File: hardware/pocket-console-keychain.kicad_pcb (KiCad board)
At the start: 2 copper layers, 52 x 76 mm, 15 parts, among them J1 USB-C Power

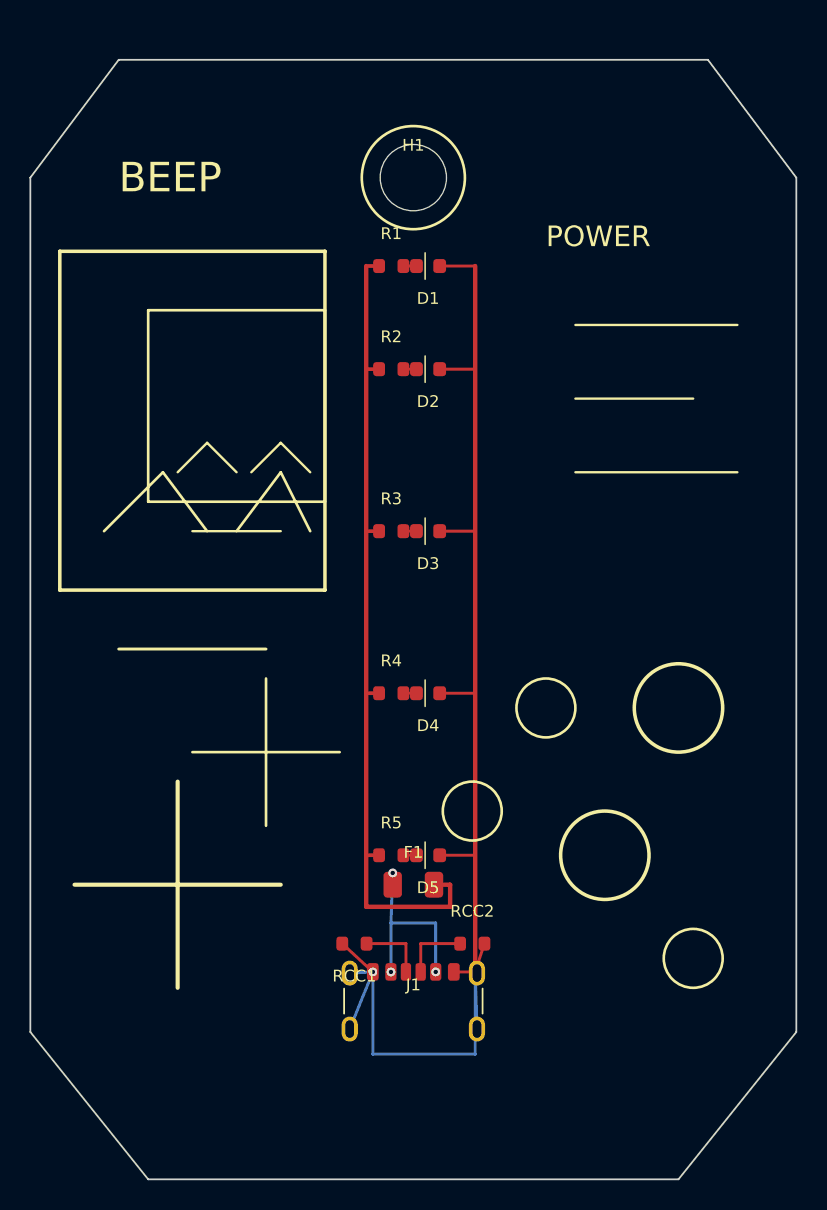
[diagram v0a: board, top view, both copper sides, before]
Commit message: Replace retro console with cleaner pocket console PCB
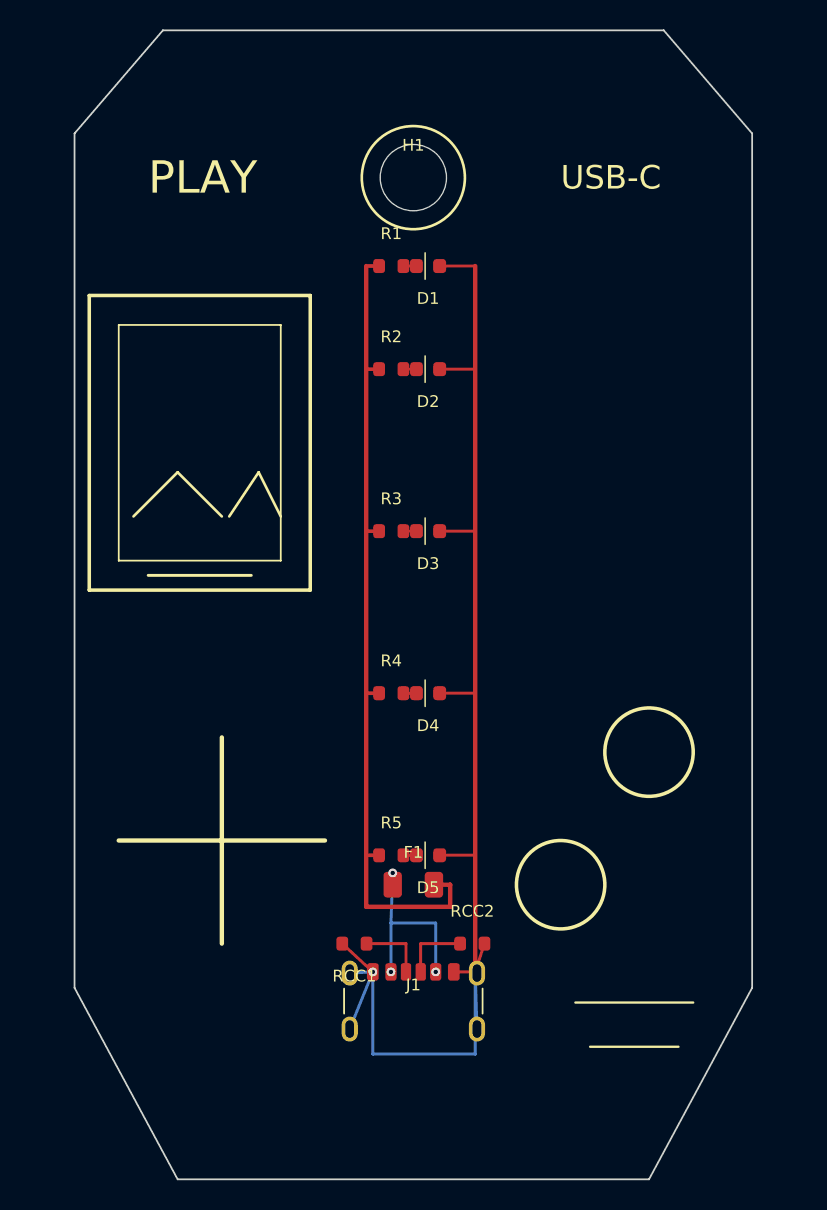
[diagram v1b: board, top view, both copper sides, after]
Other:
- board size 52 x 76 mm -> 46 x 78 mm
- board text added: "PLAY"
- board text added: "USB-C"
- board text removed: "BEEP"
- board text removed: "POWER"
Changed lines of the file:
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@@
   (paper "A4")
   (title_block
-    (title "USB-C Retro Console PCB Keychain")
+    (title "USB-C Pocket Console PCB Keychain")
     (date "2026-07-27")
     (rev "B")
     (company "Open hardware concept")
-    (comment 1 "USB-C powered retro handheld PCB keychain")
+    (comment 1 "USB-C powered pocket-console LED keychain")
   )
   (layers
@@
     (pad "2" smd roundrect (at 0.7875 0) (size 0.875 0.95) (layers "F.Cu" "F.Paste" "F.Mask") (net 10 "LED5") (pinfunction "A") (roundrect_rratio 0.25))
   )
-  (gr_line (start 56 34) (end 62 26) (stroke (width 0.12) (type solid)) (layer "Edge.Cuts") (tstamp "r0000000-0000-4000-8000-000000000001"))
-  (gr_line (start 62 26) (end 102 26) (stroke (width 0.12) (type solid)) (layer "Edge.Cuts") (tstamp "r0000000-0000-4000-8000-000000000002"))
-  (gr_line (start 102 26) (end 108 34) (stroke (width 0.12) (type solid)) (layer "Edge.Cuts") (tstamp "r0000000-0000-4000-8000-000000000003"))
-  (gr_line (start 108 34) (end 108 92) (stroke (width 0.12) (type solid)) (layer "Edge.Cuts") (tstamp "r0000000-0000-4000-8000-000000000004"))
-  (gr_line (start 108 92) (end 100 102) (stroke (width 0.12) (type solid)) (layer "Edge.Cuts") (tstamp "r0000000-0000-4000-8000-000000000005"))
-  (gr_line (start 100 102) (end 64 102) (stroke (width 0.12) (type solid)) (layer "Edge.Cuts") (tstamp "r0000000-0000-4000-8000-000000000006"))
-  (gr_line (start 64 102) (end 56 92) (stroke (width 0.12) (type solid)) (layer "Edge.Cuts") (tstamp "r0000000-0000-4000-8000-000000000007"))
-  (gr_line (start 56 92) (end 56 34) (stroke (width 0.12) (type solid)) (layer "Edge.Cuts") (tstamp "r0000000-0000-4000-8000-000000000008"))  (gr_rect (start 64 43) (end 76 56) (stroke (width 0.18) (type solid)) (fill none) (layer "F.SilkS") (tstamp "r1000000-0000-4000-8000-000000000001"))
-  (gr_line (start 66 54) (end 68 52) (stroke (width 0.16) (type solid)) (layer "F.SilkS") (tstamp "r1000000-0000-4000-8000-000000000002"))
-  (gr_line (start 68 52) (end 70 54) (stroke (width 0.16) (type solid)) (layer "F.SilkS") (tstamp "r1000000-0000-4000-8000-000000000003"))
-  (gr_line (start 71 54) (end 73 52) (stroke (width 0.16) (type solid)) (layer "F.SilkS") (tstamp "r1000000-0000-4000-8000-000000000004"))
-  (gr_line (start 73 52) (end 75 54) (stroke (width 0.16) (type solid)) (layer "F.SilkS") (tstamp "r1000000-0000-4000-8000-000000000005"))
-  (gr_line (start 67 58) (end 73 58) (stroke (width 0.16) (type solid)) (layer "F.SilkS") (tstamp "r1000000-0000-4000-8000-000000000006"))
-  (gr_line (start 72 68) (end 72 78) (stroke (width 0.18) (type solid)) (layer "F.SilkS") (tstamp "r1000000-0000-4000-8000-000000000007"))
-  (gr_line (start 67 73) (end 77 73) (stroke (width 0.18) (type solid)) (layer "F.SilkS") (tstamp "r1000000-0000-4000-8000-000000000008"))
-  (gr_circle (center 91 70) (end 93 70) (stroke (width 0.18) (type solid)) (fill none) (layer "F.SilkS") (tstamp "r1000000-0000-4000-8000-000000000009"))
-  (gr_circle (center 86 77) (end 88 77) (stroke (width 0.18) (type solid)) (fill none) (layer "F.SilkS") (tstamp "r1000000-0000-4000-8000-000000000010"))
-  (gr_rect (start 58 39) (end 76 62) (stroke (width 0.24) (type solid)) (fill none) (layer "F.SilkS") (tstamp "r3000000-0000-4000-8000-000000000001"))
-  (gr_line (start 61 58) (end 65 54) (stroke (width 0.18) (type solid)) (layer "F.SilkS") (tstamp "r3000000-0000-4000-8000-000000000002"))
-  (gr_line (start 65 54) (end 68 58) (stroke (width 0.18) (type solid)) (layer "F.SilkS") (tstamp "r3000000-0000-4000-8000-000000000003"))
-  (gr_line (start 70 58) (end 73 54) (stroke (width 0.18) (type solid)) (layer "F.SilkS") (tstamp "r3000000-0000-4000-8000-000000000004"))
-  (gr_line (start 73 54) (end 75 58) (stroke (width 0.18) (type solid)) (layer "F.SilkS") (tstamp "r3000000-0000-4000-8000-000000000005"))
-  (gr_line (start 62 66) (end 72 66) (stroke (width 0.20) (type solid)) (layer "F.SilkS") (tstamp "r3000000-0000-4000-8000-000000000006"))
-  (gr_line (start 66 75) (end 66 89) (stroke (width 0.28) (type solid)) (layer "F.SilkS") (tstamp "r3000000-0000-4000-8000-000000000007"))
-  (gr_line (start 59 82) (end 73 82) (stroke (width 0.28) (type solid)) (layer "F.SilkS") (tstamp "r3000000-0000-4000-8000-000000000008"))
-  (gr_circle (center 100 70) (end 103 70) (stroke (width 0.24) (type solid)) (fill none) (layer "F.SilkS") (tstamp "r3000000-0000-4000-8000-000000000009"))
-  (gr_circle (center 95 80) (end 98 80) (stroke (width 0.24) (type solid)) (fill none) (layer "F.SilkS") (tstamp "r3000000-0000-4000-8000-000000000010"))
-  (gr_circle (center 101 87) (end 103 87) (stroke (width 0.18) (type solid)) (fill none) (layer "F.SilkS") (tstamp "r3000000-0000-4000-8000-000000000011"))
-  (gr_line (start 93 44) (end 104 44) (stroke (width 0.16) (type solid)) (layer "F.SilkS") (tstamp "r3000000-0000-4000-8000-000000000012"))
-  (gr_line (start 93 49) (end 101 49) (stroke (width 0.16) (type solid)) (layer "F.SilkS") (tstamp "r3000000-0000-4000-8000-000000000013"))
-  (gr_line (start 93 54) (end 104 54) (stroke (width 0.16) (type solid)) (layer "F.SilkS") (tstamp "r3000000-0000-4000-8000-000000000014"))
-  (gr_text "BEEP" (at 62 34 0) (layer "F.SilkS") (tstamp "r3000000-0000-4000-8000-000000000015") (effects (font (size 2 2) (thickness 0.25)) (justify left)))
-  (gr_text "POWER" (at 91 38 0) (layer "F.SilkS") (tstamp "r3000000-0000-4000-8000-000000000016") (effects (font (size 1.4 1.4) (thickness 0.18)) (justify left)))(via (at 80.48 87.92) (size 0.6) (drill 0.3) (layers "F.Cu" "B.Cu") (net 2))
+  (gr_line (start 59 31) (end 65 24) (stroke (width 0.12) (type solid)) (layer "Edge.Cuts"))
+  (gr_line (start 65 24) (end 99 24) (stroke (width 0.12) (type solid)) (layer "Edge.Cuts"))
+  (gr_line (start 99 24) (end 105 31) (stroke (width 0.12) (type solid)) (layer "Edge.Cuts"))
+  (gr_line (start 105 31) (end 105 89) (stroke (width 0.12) (type solid)) (layer "Edge.Cuts"))
+  (gr_line (start 105 89) (end 98 102) (stroke (width 0.12) (type solid)) (layer "Edge.Cuts"))
+  (gr_line (start 98 102) (end 66 102) (stroke (width 0.12) (type solid)) (layer "Edge.Cuts"))
+  (gr_line (start 66 102) (end 59 89) (stroke (width 0.12) (type solid)) (layer "Edge.Cuts"))
+  (gr_line (start 59 89) (end 59 31) (stroke (width 0.12) (type solid)) (layer "Edge.Cuts"))  (gr_rect (start 60 42) (end 75 62) (stroke (width 0.24) (type solid)) (fill none) (layer "F.SilkS"))
+  (gr_rect (start 62 44) (end 73 60) (stroke (width 0.12) (type solid)) (fill none) (layer "F.SilkS"))
+  (gr_line (start 63 57) (end 66 54) (stroke (width 0.18) (type solid)) (layer "F.SilkS"))
+  (gr_line (start 66 54) (end 69 57) (stroke (width 0.18) (type solid)) (layer "F.SilkS"))
+  (gr_line (start 69.5 57) (end 71.5 54) (stroke (width 0.18) (type solid)) (layer "F.SilkS"))
+  (gr_line (start 71.5 54) (end 73 57) (stroke (width 0.18) (type solid)) (layer "F.SilkS"))
+  (gr_line (start 64 61) (end 71 61) (stroke (width 0.20) (type solid)) (layer "F.SilkS"))
+  (gr_line (start 69 72) (end 69 86) (stroke (width 0.30) (type solid)) (layer "F.SilkS"))
+  (gr_line (start 62 79) (end 76 79) (stroke (width 0.30) (type solid)) (layer "F.SilkS"))
+  (gr_circle (center 98 73) (end 101 73) (stroke (width 0.24) (type solid)) (fill none) (layer "F.SilkS"))
+  (gr_circle (center 92 82) (end 95 82) (stroke (width 0.24) (type solid)) (fill none) (layer "F.SilkS"))
+  (gr_line (start 93 90) (end 101 90) (stroke (width 0.16) (type solid)) (layer "F.SilkS"))
+  (gr_line (start 94 93) (end 100 93) (stroke (width 0.16) (type solid)) (layer "F.SilkS"))
+  (gr_text "PLAY" (at 64 34 0) (layer "F.SilkS") (effects (font (size 2.2 2.2) (thickness 0.28)) (justify left)))
+  (gr_text "USB-C" (at 92 34 0) (layer "F.SilkS") (effects (font (size 1.6 1.6) (thickness 0.20)) (justify left)))  (via (at 80.48 87.92) (size 0.6) (drill 0.3) (layers "F.Cu" "B.Cu") (net 2))
   (via (at 83.52 87.92) (size 0.6) (drill 0.3) (layers "F.Cu" "B.Cu") (net 2))
   (via (at 80.6 81.2) (size 0.6) (drill 0.3) (layers "F.Cu" "B.Cu") (net 2))
